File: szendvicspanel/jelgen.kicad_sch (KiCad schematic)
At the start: 11 parts, among them U1 TL072, U2 TL072

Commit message: Footprintek
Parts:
- removed R4: R_Variable, symbol Device:R_Variable
- added RV3: R_Potentiometer, Potentiometer_THT:Potentiometer_Vishay_T93YA_Vertical, symbol Device:R_Potentiometer
- C1, C2: footprint (none) -> Capacitor_THT:C_Axial_L3.8mm_D2.6mm_P7.50mm_Horizontal
- R1, R2, R3, R5: footprint (none) -> Resistor_THT:R_Axial_DIN0204_L3.6mm_D1.6mm_P5.08mm_Horizontal
- RV1, RV2: footprint (none) -> Potentiometer_THT:Potentiometer_Vishay_T93YA_Vertical
- U1, U2: footprint (none) -> Package_DIP:DIP-8_W7.62mm
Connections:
- net at R3.2, RV1.3, U1.7: now also RV3.1
- net at R1.1: now also RV3.2
- no-connect marks 0 -> 1
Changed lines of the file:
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@@
 		(color 0 0 0 0)
 	)
+	(no_connect
+		(at 123.19 124.46)
+	)
 	(wire
 		(pts
@@
 	(wire
 		(pts
-			(xy 99.06 97.79) (xy 99.06 124.46)
-		)
-		(stroke
-			(width 0)
-			(type default)
-		)
-	)
-	(wire
-		(pts
 			(xy 121.92 69.85) (xy 78.74 69.85)
 		)
@@
 	(wire
 		(pts
+			(xy 123.19 124.46) (xy 132.08 124.46)
+		)
+		(stroke
+			(width 0)
+			(type default)
+		)
+	)
+	(wire
+		(pts
 			(xy 78.74 100.33) (xy 78.74 88.9)
 		)
@@
 	(wire
 		(pts
+			(xy 99.06 97.79) (xy 99.06 128.27)
+		)
+		(stroke
+			(width 0)
+			(type default)
+		)
+	)
+	(wire
+		(pts
 			(xy 156.21 77.47) (xy 168.91 77.47)
 		)
@@
 	(wire
 		(pts
-			(xy 99.06 124.46) (xy 132.08 124.46)
-		)
-		(stroke
-			(width 0)
-			(type default)
-		)
-	)
-	(wire
-		(pts
 			(xy 49.53 86.36) (xy 63.5 86.36)
 		)
@@
 		(pts
 			(xy 121.92 43.18) (xy 121.92 69.85)
+		)
+		(stroke
+			(width 0)
+			(type default)
+		)
+	)
+	(wire
+		(pts
+			(xy 135.89 128.27) (xy 99.06 128.27)
 		)
 		(stroke
@@
 	)
 	(symbol
+		(lib_id "Device:R_Potentiometer")
+		(at 135.89 124.46 270)
+		(unit 1)
+		(exclude_from_sim no)
+		(in_bom yes)
+		(on_board yes)
+		(dnp no)
+		(fields_autoplaced yes)
+		(property "Reference" "RV3"
+			(at 135.89 118.11 90)
+			(effects
+				(font
+					(size 1.27 1.27)
+				)
+			)
+		)
+		(property "Value" "R_Potentiometer"
+			(at 135.89 120.65 90)
+			(effects
+				(font
+					(size 1.27 1.27)
+				)
+			)
+		)
+		(property "Footprint" "Potentiometer_THT:Potentiometer_Vishay_T93YA_Vertical"
+			(at 135.89 124.46 0)
+			(effects
+				(font
+					(size 1.27 1.27)
+				)
+				(hide yes)
+			)
+		)
+		(property "Datasheet" "~"
+			(at 135.89 124.46 0)
+			(effects
+				(font
+					(size 1.27 1.27)
+				)
+				(hide yes)
+			)
+		)
+		(property "Description" "Potentiometer"
+			(at 135.89 124.46 0)
+			(effects
+				(font
+					(size 1.27 1.27)
+				)
+				(hide yes)
+			)
+		)
+		(pin "1"
+		)
+		(pin "3"
+		)
+		(pin "2"
+		)
+		(instances
+			(project "szendvicspanel"
+				(path "/69584044-3e78-46a7-9ace-309a005e8329/76c3ce23-0441-427c-b036-019b5956bfe7"
+					(reference "RV3")
+					(unit 1)
+				)
+			)
+		)
+	)
+	(symbol
 		(lib_id "Device:C")
 		(at 111.76 43.18 90)
@@
 			)
 		)
-		(property "Footprint" ""
+		(property "Footprint" "Capacitor_THT:C_Axial_L3.8mm_D2.6mm_P7.50mm_Horizontal"
 			(at 115.57 42.2148 0)
 			(effects
@@
 			)
 		)
-		(property "Footprint" ""
+		(property "Footprint" "Package_DIP:DIP-8_W7.62mm"
 			(at 60.96 55.88 0)
 			(effects
@@
 			)
 		)
-		(property "Footprint" ""
+		(property "Footprint" "Potentiometer_THT:Potentiometer_Vishay_T93YA_Vertical"
 			(at 45.72 86.36 0)
 			(effects
@@
 			)
 		)
-		(property "Footprint" ""
+		(property "Footprint" "Package_DIP:DIP-8_W7.62mm"
 			(at 49.53 55.88 0)
 			(effects
@@
 			)
 		)
-		(property "Footprint" ""
+		(property "Footprint" "Package_DIP:DIP-8_W7.62mm"
 			(at 71.12 88.9 0)
 			(effects
@@
 			)
 		)
-		(property "Footprint" ""
+		(property "Footprint" "Package_DIP:DIP-8_W7.62mm"
 			(at 161.29 97.79 0)
 			(effects
@@
 			)
 		)
-		(property "Footprint" ""
+		(property "Footprint" "Resistor_THT:R_Axial_DIN0204_L3.6mm_D1.6mm_P5.08mm_Horizontal"
 			(at 132.08 44.958 90)
 			(effects
@@
 			)
 		)
-		(property "Footprint" ""
+		(property "Footprint" "Package_DIP:DIP-8_W7.62mm"
 			(at 121.92 95.25 0)
 			(effects
@@
 			)
 		)
-		(property "Footprint" ""
+		(property "Footprint" "Package_DIP:DIP-8_W7.62mm"
 			(at 143.51 45.72 0)
 			(effects
@@
 			)
 		)
-		(property "Footprint" ""
+		(property "Footprint" "Resistor_THT:R_Axial_DIN0204_L3.6mm_D1.6mm_P5.08mm_Horizontal"
 			(at 140.97 97.028 90)
 			(effects
@@
 			)
 		)
-		(property "Footprint" ""
+		(property "Footprint" "Resistor_THT:R_Axial_DIN0204_L3.6mm_D1.6mm_P5.08mm_Horizontal"
 			(at 102.87 99.568 90)
 			(effects
@@
 			)
 		)
-		(property "Footprint" ""
+		(property "Footprint" "Capacitor_THT:C_Axial_L3.8mm_D2.6mm_P7.50mm_Horizontal"
 			(at 128.27 104.4448 0)
 			(effects
@@
 			)
 		)
-		(property "Footprint" ""
+		(property "Footprint" "Resistor_THT:R_Axial_DIN0204_L3.6mm_D1.6mm_P5.08mm_Horizontal"
 			(at 152.4 79.248 90)
 			(effects
@@
 				(path "/69584044-3e78-46a7-9ace-309a005e8329/76c3ce23-0441-427c-b036-019b5956bfe7"
 					(reference "R3")
-					(unit 1)
-				)
-			)
-		)
-	)
-	(symbol
-		(lib_id "Device:R_Variable")
-		(at 135.89 124.46 90)
-		(unit 1)
-		(exclude_from_sim no)
-		(in_bom yes)
-		(on_board yes)
-		(dnp no)
-		(fields_autoplaced yes)
-		(property "Reference" "R4"
-			(at 135.89 116.84 90)
-			(effects
-				(font
-					(size 1.27 1.27)
-				)
-			)
-		)
-		(property "Value" "R_Variable"
-			(at 135.89 119.38 90)
-			(effects
-				(font
-					(size 1.27 1.27)
-				)
-			)
-		)
-		(property "Footprint" ""
-			(at 135.89 126.238 90)
-			(effects
-				(font
-					(size 1.27 1.27)
-				)
-				(hide yes)
-			)
-		)
-		(property "Datasheet" "~"
-			(at 135.89 124.46 0)
-			(effects
-				(font
-					(size 1.27 1.27)
-				)
-				(hide yes)
-			)
-		)
-		(property "Description" "Variable resistor"
-			(at 135.89 124.46 0)
-			(effects
-				(font
-					(size 1.27 1.27)
-				)
-				(hide yes)
-			)
-		)
-		(pin "2"
-		)
-		(pin "1"
-		)
-		(instances
-			(project "lebegteto_analog"
-				(path "/69584044-3e78-46a7-9ace-309a005e8329/76c3ce23-0441-427c-b036-019b5956bfe7"
-					(reference "R4")
 					(unit 1)
 				)
@@
 			)
 		)
-		(property "Footprint" ""
+		(property "Footprint" "Potentiometer_THT:Potentiometer_Vishay_T93YA_Vertical"
 			(at 185.42 97.79 0)
 			(effects

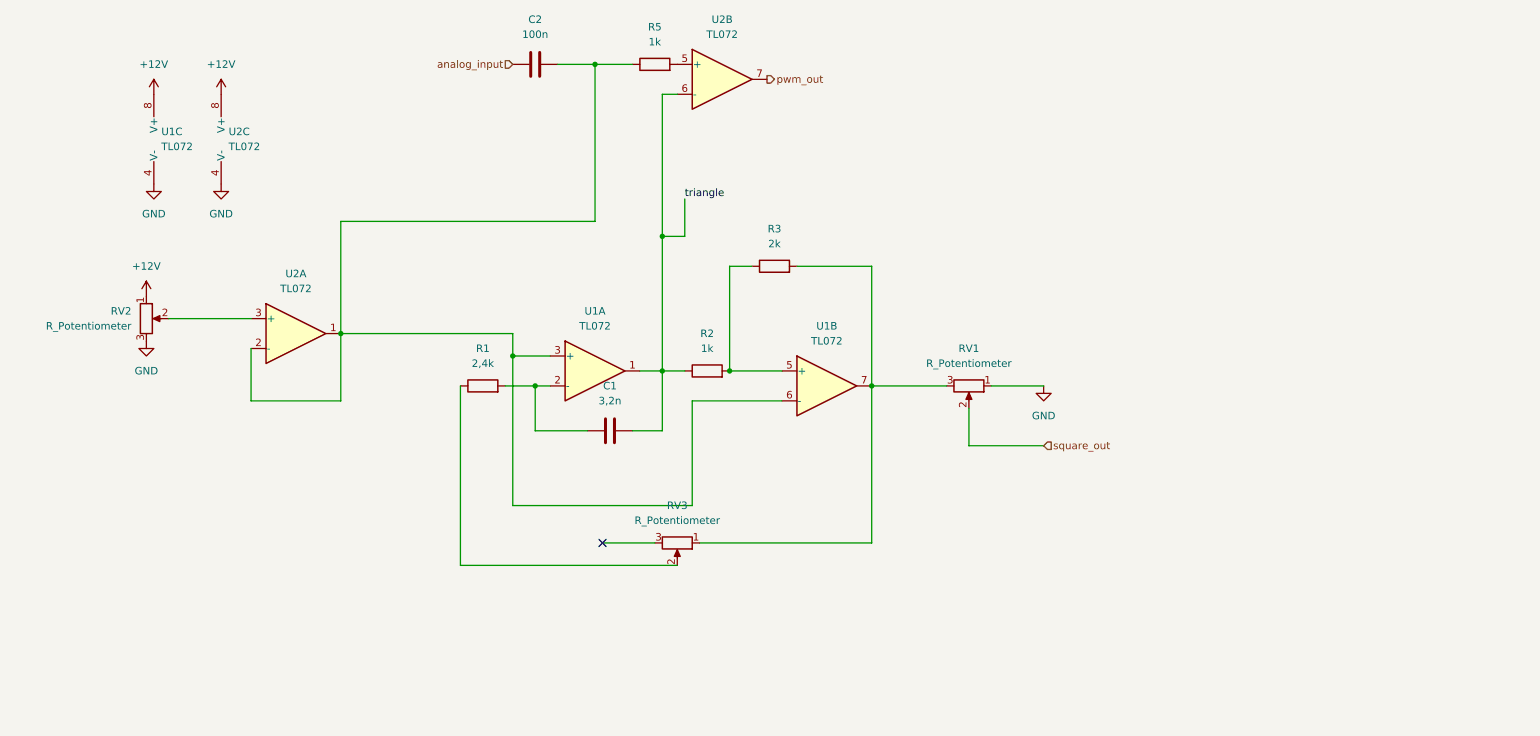
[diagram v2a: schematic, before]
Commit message: Jelgenerátor layer schematic
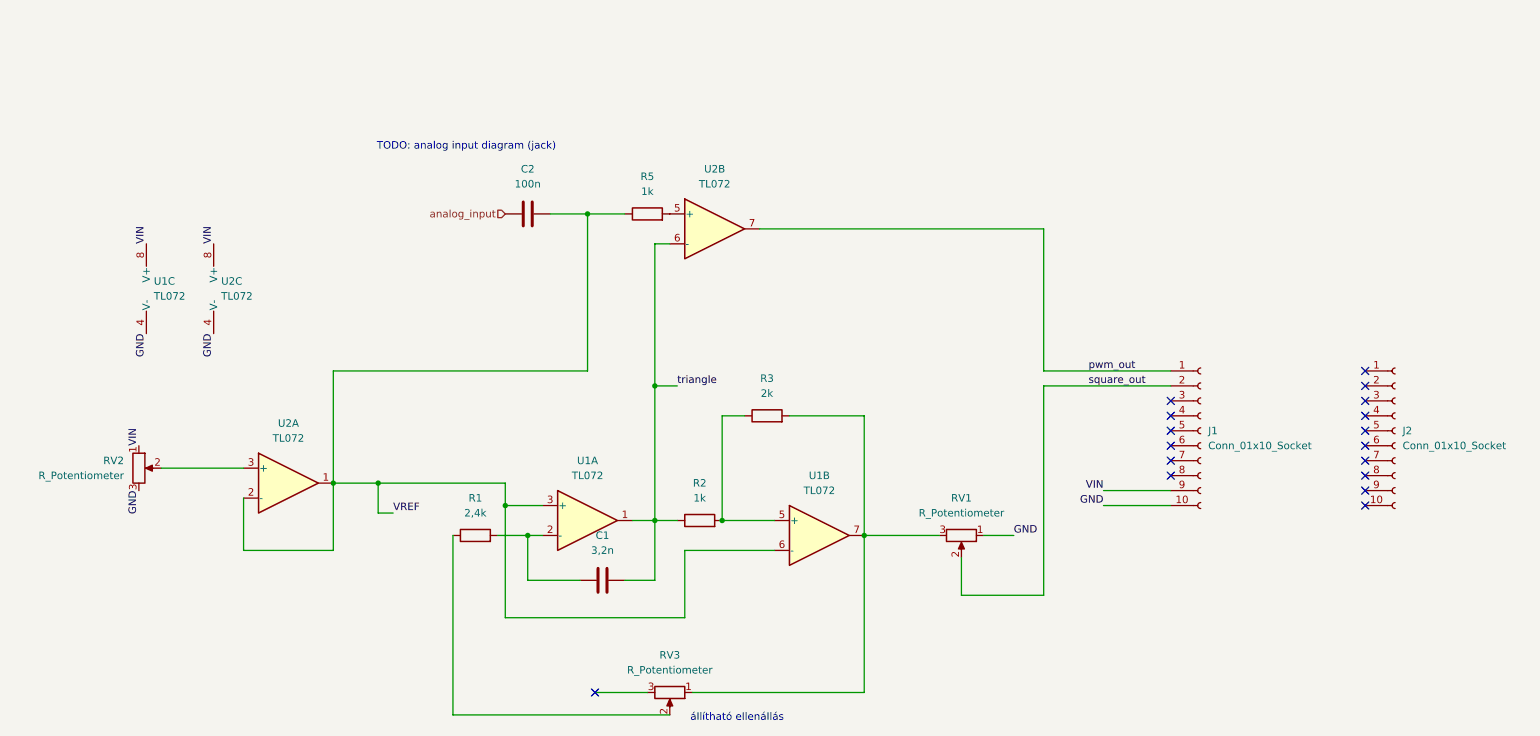
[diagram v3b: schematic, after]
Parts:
- added J1, J2: Conn_01x10_Socket, Connector_PinHeader_2.54mm:PinHeader_1x10_P2.54mm_Vertical, symbol Connector:Conn_01x10_Socket
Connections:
- net GND: now also J1.10 (Pin_10)
- net pwm_out: now also J1.1 (Pin_1)
- net square_out: now also J1.2 (Pin_2)
- net VREF: now reaches C2.2, R5.1, U1.3 (+), U1.6 (-), U2.1, U2.2 (-)
- net +12V renamed VIN
- net VIN: now also J1.9 (Pin_9)
- no-connect marks 1 -> 17
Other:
- note added: "TODO: analog input diagram (jack)"
- note added: "állítható ellenállás"
- moved on the sheet: C1, C2, R1, R2, R3, R5, RV1, RV2, RV3, U1A, U1B, U1C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

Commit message: Jelgenerátor layer, README, .gitignore
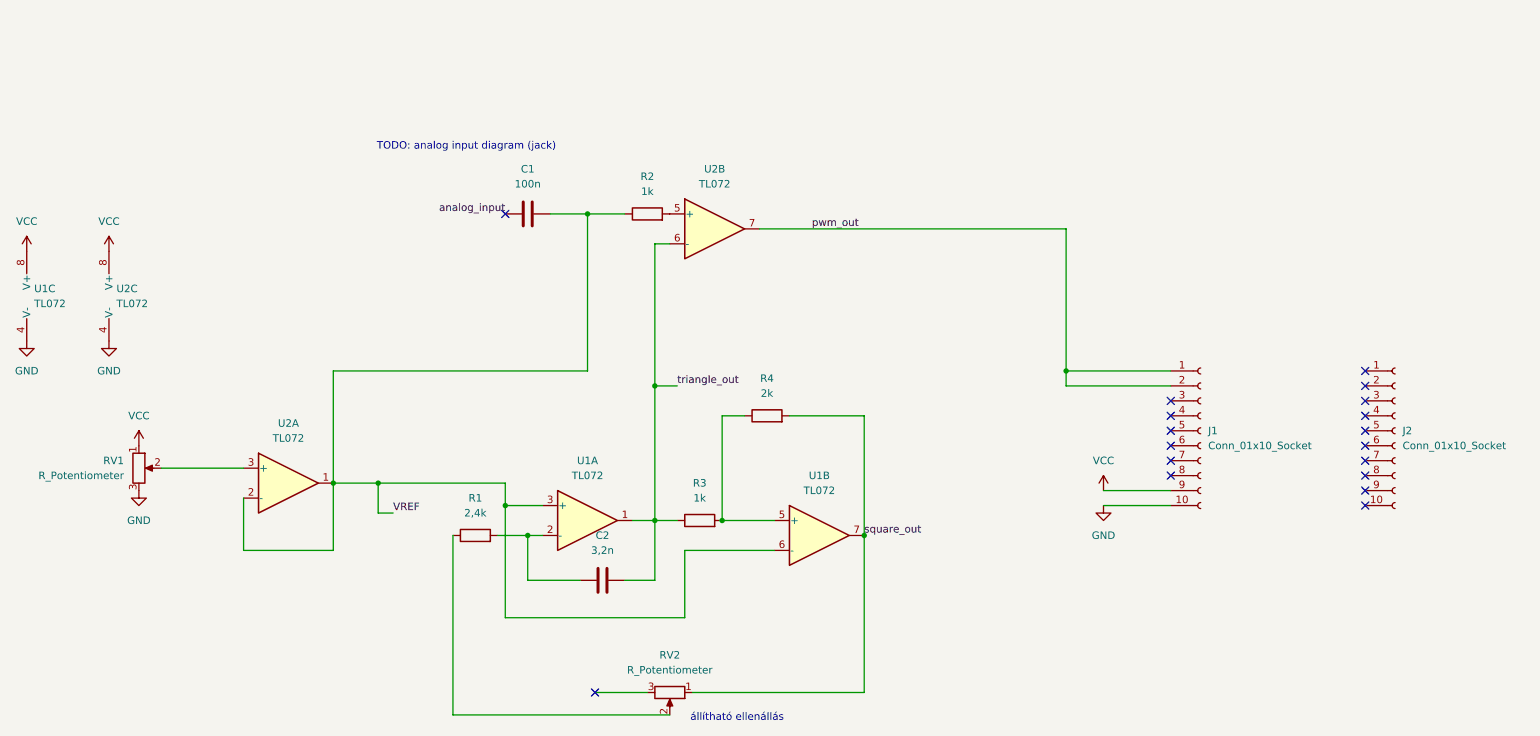
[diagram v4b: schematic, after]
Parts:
- removed RV1: R_Potentiometer, Potentiometer_THT:Potentiometer_Vishay_T93YA_Vertical, symbol Device:R_Potentiometer
- U1, U2: footprint Package_DIP:DIP-8_W7.62mm -> Package_DIP:DIP-8_W7.62mm_Socket
- renumbered C2 to C1, C1 to C2, R5 to R2, R2 to R3, R3 to R4, RV2 to RV1, RV3 to RV2
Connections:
- net pwm_out: now also J1.2 (Pin_2)
- net square_out: now also R4.2, RV2.1, U1.7; no longer J1.2 (Pin_2)
- net VIN renamed VCC
- net triangle renamed triangle_out
- no-connect marks 17 -> 18
